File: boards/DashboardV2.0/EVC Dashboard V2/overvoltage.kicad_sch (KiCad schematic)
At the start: 10 parts, among them U2 ADP3338AKCZ, U4 LTC4365CTS8-TRPBF, U5 SI9945BDY-T1-GE3, U6 SI9945BDY-T1-GE3

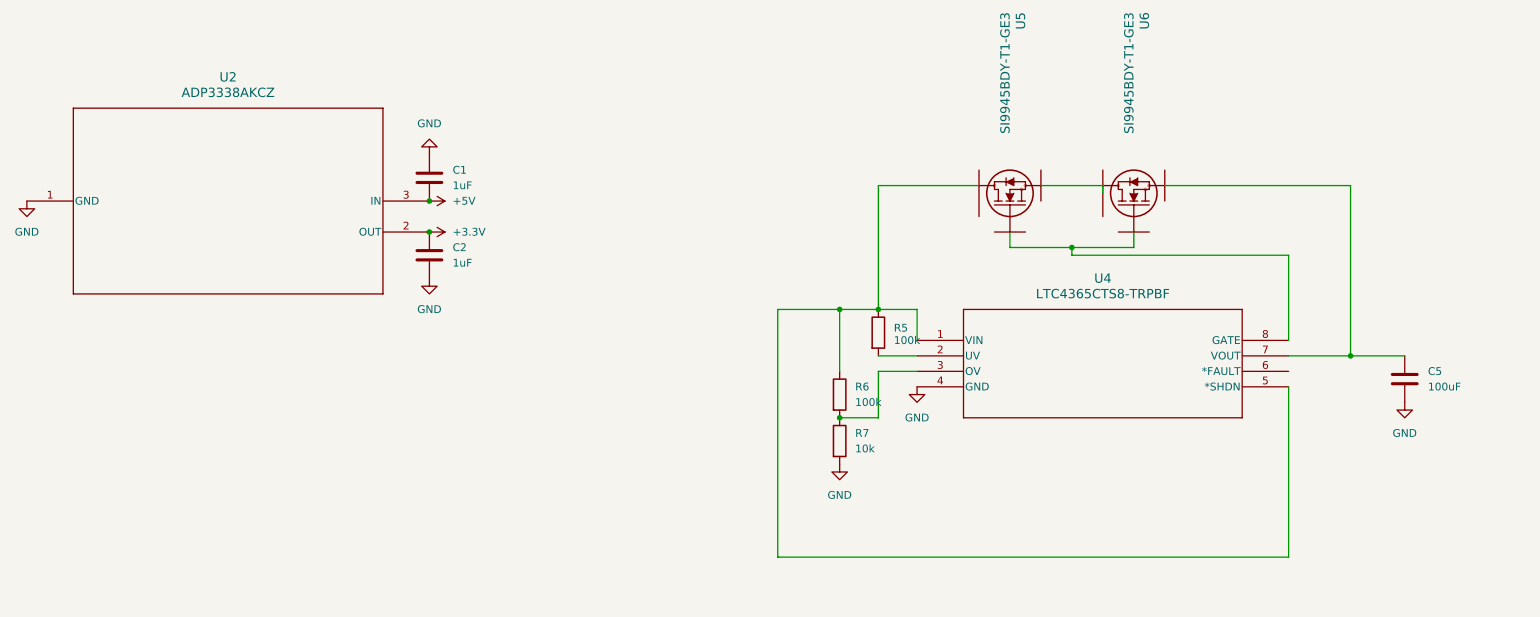
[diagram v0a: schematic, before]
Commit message: minor changes to overvoltage protection + comments
changed overvoltage protection chip wiring to better match application in datasheet, also created 5V unlimit input to separate connected 5V to the 5V running through the board (output from overvoltage circuit). also added comments on overvoltage circuit and stlink regarding confusions
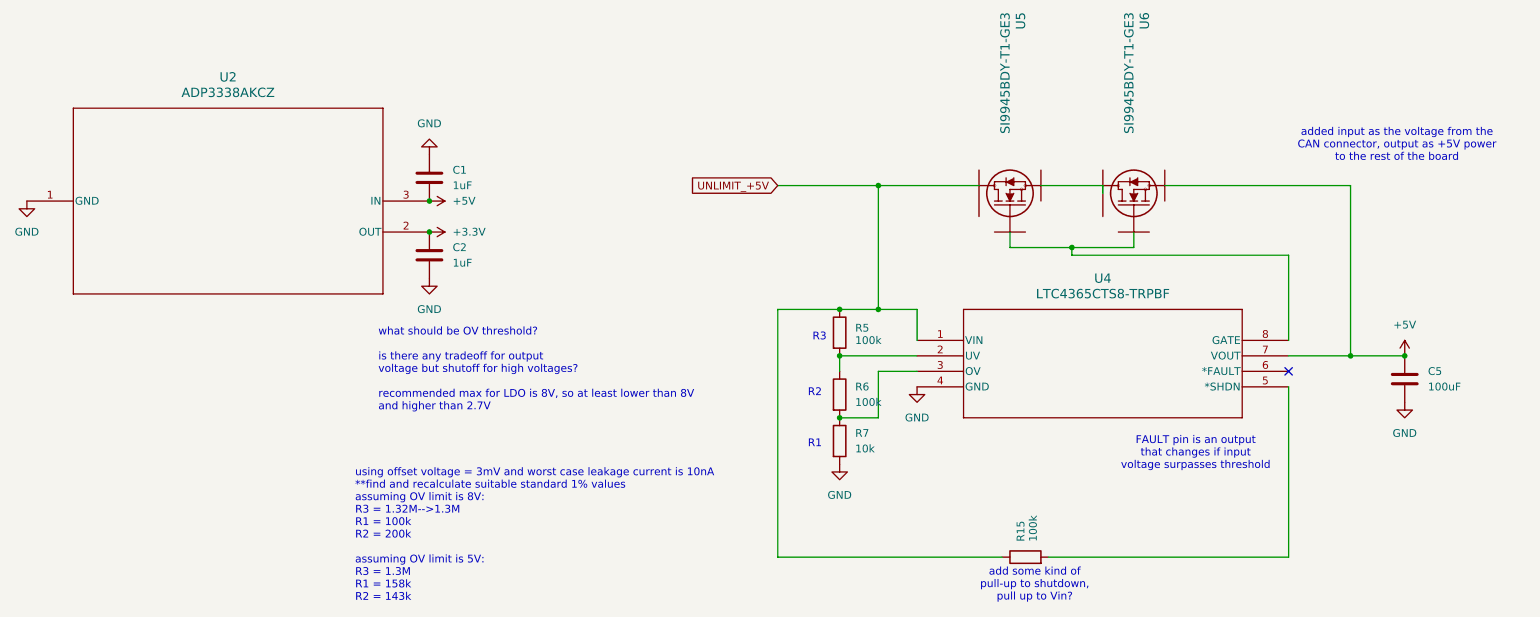
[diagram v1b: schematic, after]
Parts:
- added R15: 100k, symbol Device:R
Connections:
- net +5V: now also C5.1, U4.7 (VOUT)
- net UNLIMIT_+5V: now reaches R5.1, U4.1 (VIN)
- net UNLIMIT_+5V: now also R15.1; no longer R6.1, U4.5 (*SHDN)
- net at R5.2, U4.2 (UV): now also R6.1
- new net: R15.2, U4.5 (*SHDN)
- no-connect marks 0 -> 1
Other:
- note added: "FAULT pin is an output that changes if input voltage surpasses threshold"
- note added: "R1"
- note added: "R2"
- note added: "R3"
- note added: "add some kind of pull-up to shutdown, pull up to Vin?"
- note added: "added input as the voltage from the CAN connector, output as +5V power to the rest of the board"
- note added: "using offset voltage = 3mV and worst case leakage current is 10nA **find and recalculate suitable standard 1% values assuming OV limit is 8V: R3 = 1.32M-->1.3M R1 = 100k R2 = 200k assuming OV limit is 5V: R3 = 1.3M R1 = 158k R2 = 143k"
- note added: "what should be OV threshold? is there any tradeoff for output voltage but shutoff for high voltages? recommended max for LDO is 8V, so at least lower than 8V and higher than 2.7V"
